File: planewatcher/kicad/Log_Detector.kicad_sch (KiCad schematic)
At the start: 17 parts, among them U9 ADL5513

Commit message: change discontinued parts
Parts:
- C42, C43: MPN GRM155R71A473KA01D -> CC0402KRX7R6BB473; Manufacturer Murata Electronics -> YAGEO; lcsc_id C113049 -> C327054
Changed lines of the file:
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@@
 			)
 		)
-		(property "MPN" "GRM155R71A473KA01D"
+		(property "MPN" "CC0402KRX7R6BB473"
 			(at 130.81 69.85 0)
 			(hide yes)
@@
 			)
 		)
-		(property "Manufacturer" "Murata Electronics"
+		(property "Manufacturer" "YAGEO"
 			(at 130.81 69.85 0)
 			(hide yes)
@@
 			)
 		)
-		(property "lcsc_id" "C113049"
+		(property "lcsc_id" "C327054"
 			(at 130.81 69.85 0)
 			(hide yes)
@@
 			)
 		)
-		(property "MPN" "GRM155R71A473KA01D"
+		(property "MPN" "CC0402KRX7R6BB473"
 			(at 109.22 62.23 0)
 			(hide yes)
@@
 			)
 		)
-		(property "Manufacturer" "Murata Electronics"
+		(property "Manufacturer" "YAGEO"
 			(at 109.22 62.23 0)
 			(hide yes)
@@
 			)
 		)
-		(property "lcsc_id" "C113049"
+		(property "lcsc_id" "C327054"
 			(at 109.22 62.23 0)
 			(hide yes)

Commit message: update BoM to available parts from LCSC
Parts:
- C70: MPN GRM155R71C103KA01D -> CL05B103KB5NNNC; Manufacturer Murata Electronics -> Samsung Electro-Mechanics; lcsc_id C85735 -> C15195
- R25: MPN ERA-2AEB52R3X -> RC0402FR-0752R3L; Manufacturer Panasonic Industry -> YAGEO; lcsc_id C2088289 -> C273696
- R26: MPN ERA-2ARB2672X -> ERJ2RKF2672X; Manufacturer Panasonic Industry -> PANASONIC; lcsc_id C4221522 -> C2077115
- R27: MPN ERA-2ARB8451X -> RT0402BRD078K45L; Manufacturer Panasonic Industry -> YAGEO; lcsc_id C4151733 -> C728566
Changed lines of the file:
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@@
 			)
 		)
-		(property "MPN" "GRM155R71C103KA01D"
+		(property "MPN" "CL05B103KB5NNNC"
 			(at 203.2 91.44 0)
 			(hide yes)
@@
 			)
 		)
-		(property "Manufacturer" "Murata Electronics"
+		(property "Manufacturer" "Samsung Electro-Mechanics"
 			(at 203.2 91.44 0)
 			(hide yes)
@@
 			)
 		)
-		(property "lcsc_id" "C85735"
+		(property "lcsc_id" "C15195"
 			(at 203.2 91.44 0)
 			(hide yes)
@@
 			)
 		)
-		(property "MPN" "ERA-2ARB2672X"
+		(property "MPN" "ERJ2RKF2672X"
 			(at 220.98 96.52 0)
 			(hide yes)
@@
 			)
 		)
-		(property "Manufacturer" "Panasonic Industry"
+		(property "Manufacturer" "PANASONIC"
 			(at 220.98 96.52 0)
 			(hide yes)
@@
 			)
 		)
-		(property "lcsc_id" "C4221522"
+		(property "lcsc_id" "C2077115"
 			(at 220.98 96.52 0)
 			(hide yes)
@@
 			)
 		)
-		(property "MPN" "ERA-2ARB8451X"
+		(property "MPN" "RT0402BRD078K45L"
 			(at 214.63 114.3 0)
 			(hide yes)
@@
 			)
 		)
-		(property "Manufacturer" "Panasonic Industry"
+		(property "Manufacturer" "YAGEO"
 			(at 214.63 114.3 0)
 			(hide yes)
@@
 			)
 		)
-		(property "lcsc_id" "C4151733"
+		(property "lcsc_id" "C728566"
 			(at 214.63 114.3 0)
 			(hide yes)
@@
 			)
 		)
-		(property "Description" "52.3 Ohms ±0.1% 0.063W, 1/16W Chip Resistor 0402 (1005 Metric) Automotive AEC-Q200 Thin Film"
+		(property "Description" "62.5mW 52.3Ω 50V Thick Film Resistor ±100ppm/℃ ±1% 0402 Chip Resistor - Surface Mount RoHS"
 			(at 101.6 66.04 0)
 			(hide yes)
@@
 			)
 		)
-		(property "MPN" "ERA-2AEB52R3X"
+		(property "MPN" "RC0402FR-0752R3L"
 			(at 101.6 66.04 0)
 			(hide yes)
@@
 			)
 		)
-		(property "Manufacturer" "Panasonic Industry"
+		(property "Manufacturer" "YAGEO"
 			(at 101.6 66.04 0)
 			(hide yes)
@@
 			)
 		)
-		(property "lcsc_id" "C2088289"
+		(property "lcsc_id" "C273696"
 			(at 101.6 66.04 0)
 			(hide yes)

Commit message: better footprint for log detector
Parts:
- U9: footprint Package_CSP:LFCSP-16-1EP_3x3mm_P0.5mm_EP1.854x1.854mm -> Package_CSP:LFCSP-16-1EP_3x3mm_P0.5mm_EP1.6x1.6mm
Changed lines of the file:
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@@
 			)
 		)
-		(property "Footprint" "Package_CSP:LFCSP-16-1EP_3x3mm_P0.5mm_EP1.854x1.854mm"
+		(property "Footprint" "Package_CSP:LFCSP-16-1EP_3x3mm_P0.5mm_EP1.6x1.6mm"
 			(at 175.26 50.8 0)
 			(hide yes)

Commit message: Add footprints for ADL5513 slope adjustment and output filtering
- Add R44 (0Ω) & R45 (DNP, footprint only), allowing for replacement to adjust slope.
- Add C61 (DNP, footprint only), allowing for output filtering to reduce output bandwidth if needed.
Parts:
- added C61: 100pF, Capacitor_SMD:C_0402_1005Metric, symbol Device:C
- added R44, R45: 0Ω, Resistor_SMD:R_0402_1005Metric, symbol Device:R
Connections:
- net GND: now also C61.1, R45.2
- net VLOG_OUT: now also R44.1; no longer U9.11 (VSET)
- net at U9.14 (CLPF): now also C61.2
- new net: R44.2, R45.1, U9.11 (VSET)
- no-connect marks 1 -> 0
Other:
- note added: "Datasheet says to operate in measurement mode, connect VOUT to VSET. Footprints added so we can experiment with slope adjustment."
- note removed: "Datasheet says to operate in measurement mode, connect VOUT to VSET."

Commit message: Update BoM
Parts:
- R41, R42: MPN CRCW0402 (TBD) -> (none); Manufacturer Vishay -> (none); Package 0402 -> 0402 (1005 Metric)
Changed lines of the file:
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@@
 			)
 		)
-		(property "Package" "0402"
+		(property "Package" "0402 (1005 Metric)"
 			(at 52.07 67.31 0)
 			(hide yes)
@@
 			)
 		)
-		(property "MPN" "CRCW0402 (TBD)"
+		(property "MPN" ""
 			(at 52.07 67.31 0)
 			(hide yes)
@@
 			)
 		)
-		(property "Manufacturer" "Vishay"
+		(property "Manufacturer" ""
 			(at 52.07 67.31 0)
 			(hide yes)
@@
 			)
 		)
-		(property "Package" "0402"
+		(property "Package" "0402 (1005 Metric)"
 			(at 67.31 67.31 0)
 			(hide yes)
@@
 			)
 		)
-		(property "MPN" "CRCW0402 (TBD)"
+		(property "MPN" ""
 			(at 67.31 67.31 0)
 			(hide yes)
@@
 			)
 		)
-		(property "Manufacturer" "Vishay"
+		(property "Manufacturer" ""
 			(at 67.31 67.31 0)
 			(hide yes)

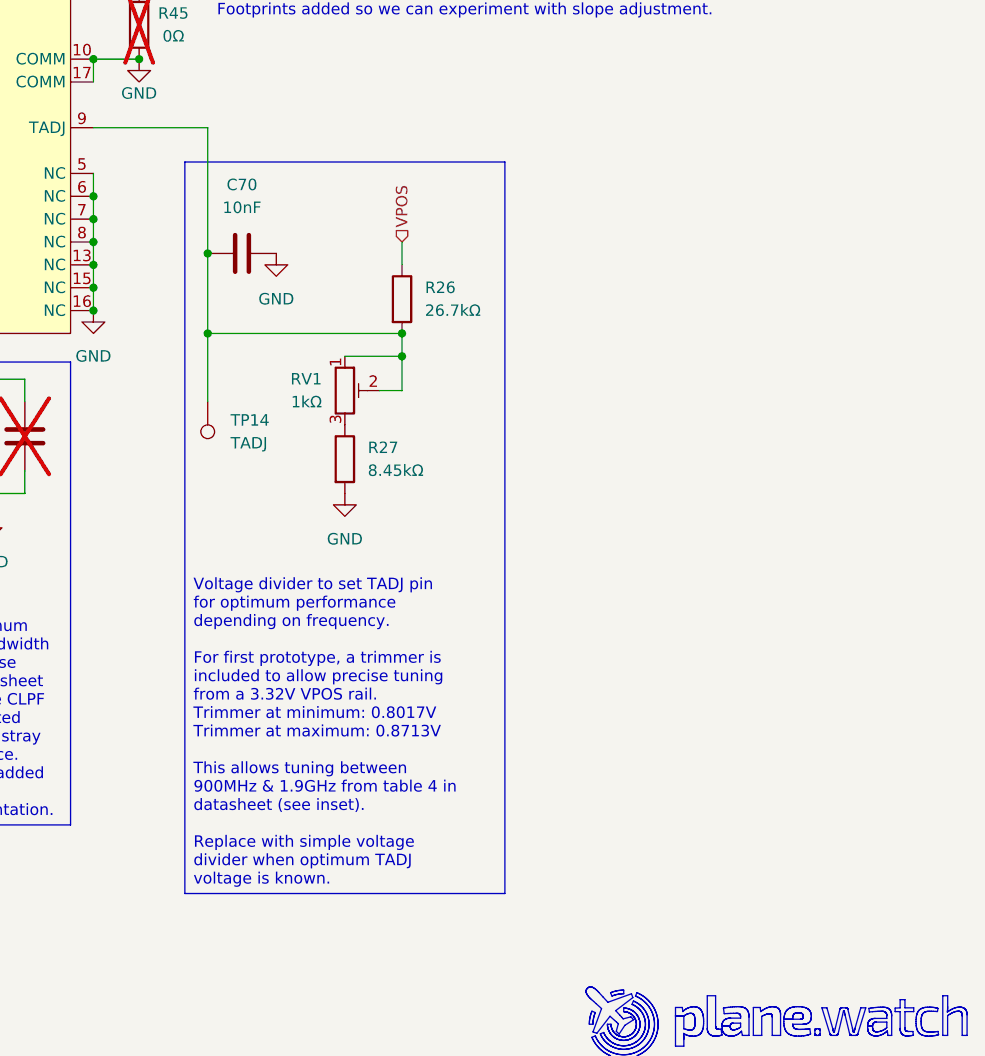
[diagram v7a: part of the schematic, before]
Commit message: Replace TADJ prototype trimmer with voltage divider
Voltage divider sets the ADL5513 TADJ pin to approximately 0.85 V for 1090 MHz operation
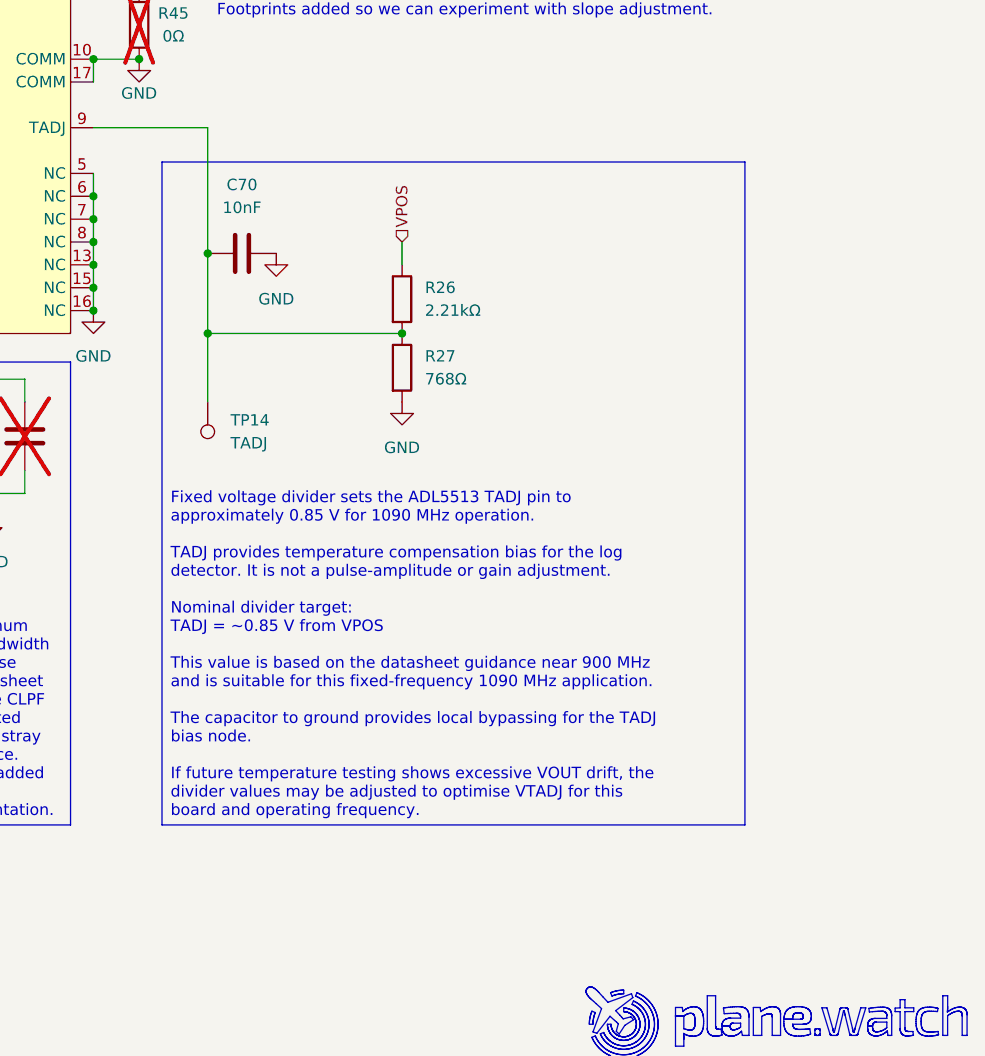
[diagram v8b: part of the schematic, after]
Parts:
- removed RV1: 1kΩ, Potentiometer_SMD:Potentiometer_Bourns_3224W_Vertical, symbol Device:R_Potentiometer_Trim
- R26: value 26.7kΩ -> 2.21kΩ; MPN ERJ2RKF2672X -> ERJ2RKF2211X; Package 0402 (1005 Metric) -> 0402 (1005 Metric); Purpose Upper resistor in the ADL5513 TADJ divider for 1090MHz dete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 -> Upper resistor in the ADL5513 TADJ divider; lcsc_id C2077115 -> C416496
- R27: value 8.45kΩ -> 768Ω; MPN RT0402BRD078K45L -> ERJ2RKF7680X; Manufacturer YAGEO -> PANASONIC; Purpose Lower resistor in the ADL5513 TADJ divider for 1090MHz dete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 -> Lower resistor in the ADL5513 TADJ divider; lcsc_id C728566 -> C3025660
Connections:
- net at C70.1, R26.2, TP14.1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: now also R27.1
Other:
- moved on the sheet: R27
